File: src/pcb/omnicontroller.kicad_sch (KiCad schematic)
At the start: 49 parts, among them J1 G-Switch GT-USB-7010ASV, J2 USB_A, J3 Conn_01x07_Pin, U1 RP2040, U2 NCP1117ST33T3G, U3 W25Q128JVSIM, X1 SW_Omron_B3FS-1000P, Y1 ABM8-272-T3, Y2 SW_Omron_B3FS-1000P

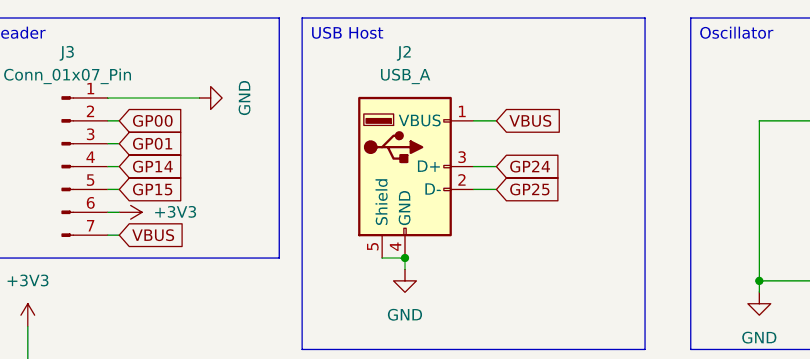
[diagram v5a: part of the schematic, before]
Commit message: update usb A connector
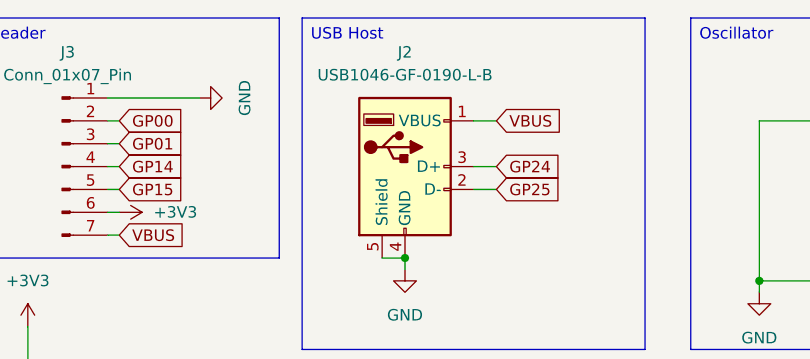
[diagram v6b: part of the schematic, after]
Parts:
- J2: value USB_A -> USB1046-GF-0190-L-B
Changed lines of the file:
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@@
 			)
 		)
-		(property "Value" "USB_A"
+		(property "Value" "USB1046-GF-0190-L-B"
 			(at 190.5 19.05 0)
 			(effects
@@
 			)
 		)
-		(property "Datasheet" "https://mm.digikey.com/Volume0/opasdata/d220001/medias/docus/5335/USB1046_Spec.pdf"
+		(property "Datasheet" "https://gct.co/connector/usb1046"
 			(at 194.31 30.48 0)
 			(effects
@@
 			)
 		)
-		(property "Description" "USB Type A connector"
+		(property "Description" "USB Type A connector GCT USB1046-GF-0190-L-B"
 			(at 190.5 29.21 0)
 			(effects
